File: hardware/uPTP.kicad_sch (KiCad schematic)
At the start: 16 parts, among them J1 PPS_UFL, J2 PPS_SMA, J3 LED, J4 UART_HDR, U1 XC6206P332MR-G

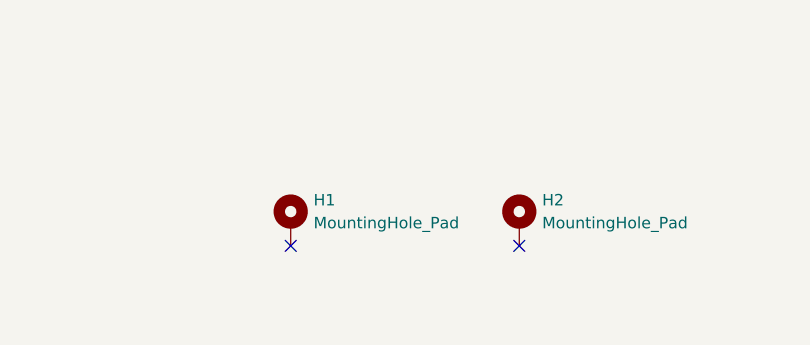
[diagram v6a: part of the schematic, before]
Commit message: ISO ETH Section Done
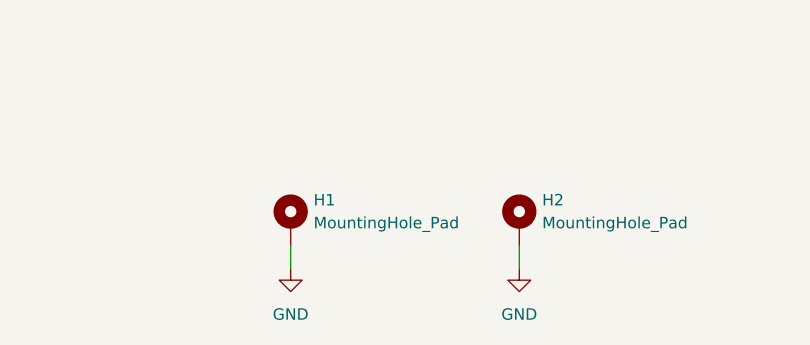
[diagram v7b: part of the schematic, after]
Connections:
- net GND: now also H1.1, H2.1
- no-connect marks 2 -> 0
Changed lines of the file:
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@@
 		(color 0 0 0 0)
 	)
-	(no_connect
-		(at 152.4 187.96)
-	)
-	(no_connect
-		(at 127 187.96)
-	)
 	(wire
 		(pts
@@
 	(wire
 		(pts
+			(xy 127 187.96) (xy 127 190.5)
+		)
+		(stroke
+			(width 0)
+			(type default)
+		)
+	)
+	(wire
+		(pts
 			(xy 115.57 59.69) (xy 123.19 59.69)
 		)
@@
 		(pts
 			(xy 138.43 69.85) (xy 134.62 69.85)
+		)
+		(stroke
+			(width 0)
+			(type default)
+		)
+	)
+	(wire
+		(pts
+			(xy 152.4 187.96) (xy 152.4 190.5)
 		)
 		(stroke
@@
 	(symbol
 		(lib_id "power:GND")
+		(at 127 190.5 0)
+		(unit 1)
+		(exclude_from_sim no)
+		(in_bom yes)
+		(on_board yes)
+		(dnp no)
+		(fields_autoplaced yes)
+		(property "Reference" "#PWR048"
+			(at 127 196.85 0)
+			(effects
+				(font
+					(size 1.27 1.27)
+				)
+				(hide yes)
+			)
+		)
+		(property "Value" "GND"
+			(at 127 195.58 0)
+			(effects
+				(font
+					(size 1.27 1.27)
+				)
+			)
+		)
+		(property "Footprint" ""
+			(at 127 190.5 0)
+			(effects
+				(font
+					(size 1.27 1.27)
+				)
+				(hide yes)
+			)
+		)
+		(property "Datasheet" ""
+			(at 127 190.5 0)
+			(effects
+				(font
+					(size 1.27 1.27)
+				)
+				(hide yes)
+			)
+		)
+		(property "Description" "Power symbol creates a global label with name \"GND\" , ground"
+			(at 127 190.5 0)
+			(effects
+				(font
+					(size 1.27 1.27)
+				)
+				(hide yes)
+			)
+		)
+		(pin "1"
+		)
+		(instances
+			(project ""
+				(path "/c29659fd-9e8d-4714-a690-4e74e6e849c2"
+					(reference "#PWR048")
+					(unit 1)
+				)
+			)
+		)
+	)
+	(symbol
+		(lib_id "power:GND")
 		(at 114.3 88.9 0)
 		(unit 1)
@@
 					(unit 1)
 				)
+			)
+		)
+	)
+	(symbol
+		(lib_id "power:GND")
+		(at 152.4 190.5 0)
+		(unit 1)
+		(exclude_from_sim no)
+		(in_bom yes)
+		(on_board yes)
+		(dnp no)
+		(fields_autoplaced yes)
+		(property "Reference" "#PWR049"
+			(at 152.4 196.85 0)
+			(effects
+				(font
+					(size 1.27 1.27)
+				)
+				(hide yes)
+			)
+		)
+		(property "Value" "GND"
+			(at 152.4 195.58 0)
+			(effects
+				(font
+					(size 1.27 1.27)
+				)
+			)
+		)
+		(property "Footprint" ""
+			(at 152.4 190.5 0)
+			(effects
+				(font
+					(size 1.27 1.27)
+				)
+				(hide yes)
+			)
+		)
+		(property "Datasheet" ""
+			(at 152.4 190.5 0)
+			(effects
+				(font
+					(size 1.27 1.27)
+				)
+				(hide yes)
+			)
+		)
+		(property "Description" "Power symbol creates a global label with name \"GND\" , ground"
+			(at 152.4 190.5 0)
+			(effects
+				(font
+					(size 1.27 1.27)
+				)
+				(hide yes)
+			)
+		)
+		(pin "1"
+		)
+		(instances
+			(project "uPTP"
+				(path "/c29659fd-9e8d-4714-a690-4e74e6e849c2"
+					(reference "#PWR049")
+					(unit 1)
+				)

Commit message: All footprints 3D plus some more routing
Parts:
- D4: LCSC Part (none) -> C965555
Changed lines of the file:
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@@
+			)
+		)
+		(property "LCSC Part" "C965555"
+			(at 254 50.8 0)
+			(effects
+				(font
+					(size 1.27 1.27)
+				)
+				(hide yes)
 			)
 		)
